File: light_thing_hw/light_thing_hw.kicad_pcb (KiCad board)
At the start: 2 copper layers, 51 parts, among them J1 CONNECTORS, J2 Li-Ion Battery, J3 ADDR_LED_PANEL_1_CONNECTORS, J4 ADDR_LED_PANEL_2_CONNECTORS, Q1 MMBF170, SW1 ST_USER_BUTTON1, SW2 ST_RESET_BUTTON, U1 BC832-V1, U2 LSM6DS3, U3 MCP73833T-FCI_MF, U4 LMR62421XMF, U5 LP38511MRX-ADJ_NOPB, U5A1 STM32L452RETx

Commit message: hw updates
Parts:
- moved J2 6.18 mm to (166.8, 80.5)
- moved SW1 4.24 mm to (155.0, 74.0)
- moved USB_MICRO_CONN1 4.24 mm to (154.9, 62.0)
- moved D2 3.16 mm to (161.0, 49.0)
- moved D3 3.16 mm to (156.9, 49.0)
- moved J1 3.16 mm to (174.0, 70.0)
- moved J3 3.16 mm to (169.0, 70.0)
- moved J4 3.16 mm to (165.0, 70.0)
- moved Q1 3.16 mm to (182.0, 63.0)
- moved SW2 3.16 mm to (160.0, 59.0)
- moved U1 3.16 mm to (176.0, 53.0)
- moved U2 3.16 mm to (181.0, 54.0)
- moved U3 3.16 mm to (181.0, 62.0)
- moved U4 3.16 mm to (180.0, 68.0)
- moved U5 3.16 mm to (182.0, 75.0)
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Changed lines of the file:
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@@
   (general
     (thickness 1.6)
-    (drawings 11)
+    (drawings 12)
     (tracks 0)
     (zones 0)
@@
   )
   (module LED_SMD:LED_1806_4516Metric_Pad1.57x1.80mm_HandSolder (layer F.Cu)
-    (at 164 50 90)
+    (at 161 49 90)
     (descr "LED SMD 1806 (4516 Metric), square (rectangular) end terminal, IPC_7351 nominal, (Body size source: https://www.modelithics.com/models/Vendor/MuRata/BLM41P.pdf), generated with kicad-footprint-generator")
     (tags "LED handsolder")
@@
   )
   (module LED_SMD:LED_1806_4516Metric_Pad1.57x1.80mm_HandSolder (layer F.Cu)
-    (at 159.9125 50 90)
+    (at 156.9125 49 90)
     (descr "LED SMD 1806 (4516 Metric), square (rectangular) end terminal, IPC_7351 nominal, (Body size source: https://www.modelithics.com/models/Vendor/MuRata/BLM41P.pdf), generated with kicad-footprint-generator")
     (tags "LED handsolder")
@@
   )
   (module Connector_Molex:Molex_PicoBlade_53261-0271_1x02-1MP_P1.25mm_Horizontal (layer B.Cu)
-    (at 172.825 79)
+    (at 166.825 80.5)
     (descr "Molex PicoBlade series connector, 53261-0271 (http://www.molex.com/pdm_docs/sd/532610271_sd.pdf), generated with kicad-footprint-generator")
     (tags "connector Molex PicoBlade top entry")
@@
   )
   (module Connector_PinHeader_1.00mm:PinHeader_2x02_P1.00mm_Vertical (layer F.Cu)
-    (at 172 71)
+    (at 169 70)
     (descr "Through hole straight pin header, 2x02, 1.00mm pitch, double rows")
     (tags "Through hole pin header THT 2x02 1.00mm double row")
@@
   )
   (module Connector_PinHeader_1.00mm:PinHeader_2x02_P1.00mm_Vertical (layer F.Cu)
-    (at 168 71)
+    (at 165 70)
     (descr "Through hole straight pin header, 2x02, 1.00mm pitch, double rows")
     (tags "Through hole pin header THT 2x02 1.00mm double row")
@@
   )
   (module Package_TO_SOT_SMD:SOT-23 (layer F.Cu)
-    (at 185 64)
+    (at 182 63)
     (descr "SOT-23, Standard")
     (tags SOT-23)
@@
   )
   (module Button_Switch_THT:SW_Tactile_SPST_Angled_PTS645Vx39-2LFS (layer B.Cu)
-    (at 158 71 270)
+    (at 155 74 270)
     (descr "tactile switch SPST right angle, PTS645VL39-2 LFS")
     (tags "tactile switch SPST angled PTS645VL39-2 LFS C&K Button")
@@
   )
   (module Button_Switch_SMD:SW_SPST_CK_RS282G05A3 (layer F.Cu)
-    (at 163 60 90)
+    (at 160 59 90)
     (descr https://www.mouser.com/ds/2/60/RS-282G05A-SM_RT-1159762.pdf)
     (tags "SPST button tactile switch")
@@
   )
   (module Package_LGA:LGA-14_3x2.5mm_P0.5mm_LayoutBorder3x4y (layer F.Cu)
-    (at 184 55)
+    (at 181 54)
     (descr "LGA, 14 Pin (http://www.st.com/resource/en/datasheet/lsm6ds3.pdf), generated with kicad-footprint-generator ipc_lga_layoutBorder_generator.py")
     (tags "LGA LGA")
@@
   )
   (module footprints:MCP73833T-FCI&slash_MF (layer B.Cu)
-    (at 184 63)
+    (at 181 62)
     (fp_text reference U3 (at 0 3) (layer B.SilkS)
       (effects (font (size 1 1) (thickness 0.15)) (justify mirror))
@@
   )
   (module Package_TO_SOT_SMD:SOT-23-5 (layer B.Cu)
-    (at 183 69)
+    (at 180 68)
     (descr "5-pin SOT23 package")
     (tags SOT-23-5)
@@
   )
   (module footprints:LP38511MRX-ADJ_NOPB (layer B.Cu)
-    (at 185 76)
+    (at 182 75)
     (fp_text reference U5 (at 0 0) (layer B.SilkS)
       (effects (font (size 1 1) (thickness 0.15)) (justify mirror))
@@
   )
   (module Package_QFP:LQFP-64-1EP_10x10mm_P0.5mm_EP6.5x6.5mm (layer F.Cu)
-    (at 174 60)
+    (at 171 59)
     (descr "64 LEAD LQFP 10x10mm (see MICREL LQFP10x10-64LD-PL-1.pdf and http://www.nxp.com/files/shared/doc/package_info/98ARH98426A.pdf for EP)")
     (tags "QFP 0.5")
@@
   )
   (module Connector_USB:USB_Micro-B_Molex_47346-0001 (layer B.Cu)
-    (at 157.9 59 90)
+    (at 154.9 62 90)
     (descr "Micro USB B receptable with flange, bottom-mount, SMD, right-angle (http://www.molex.com/pdm_docs/sd/473460001_sd.pdf)")
     (tags "Micro B USB SMD")
@@
   )
   (module Connector_PinHeader_1.00mm:PinHeader_2x05_P1.00mm_Vertical (layer F.Cu)
-    (at 177 71)
+    (at 174 70)
     (descr "Through hole straight pin header, 2x05, 1.00mm pitch, double rows")
     (tags "Through hole pin header THT 2x05 1.00mm double row")
@@
   )
   (module Fanstel_modules:BC832-BC832_3d1 (layer B.Cu)
-    (at 179 54 180)
+    (at 176 53 180)
     (attr smd)
     (fp_text reference U1 (at 4.3 9.7 180) (layer B.SilkS)
@@
     )
   )
-  (dimension 30 (width 0.3) (layer F.SilkS)
-    (gr_text "30.000 mm" (at 193.1 65 270) (layer F.SilkS)
+  (gr_line (start 151 48) (end 151 43) (layer F.SilkS) (width 0.2))
+  (gr_line (start 193 80) (end 193 85) (layer F.SilkS) (width 0.2))
+  (dimension 42 (width 0.3) (layer F.SilkS)
+    (gr_text "42.000 mm" (at 140.9 64 90) (layer F.SilkS)
       (effects (font (size 1.5 1.5) (thickness 0.3)))
     )
-    (feature1 (pts (xy 190 80) (xy 191.586421 80)))
-    (feature2 (pts (xy 190 50) (xy 191.586421 50)))
-    (crossbar (pts (xy 191 50) (xy 191 80)))
-    (arrow1a (pts (xy 191 80) (xy 190.413579 78.873496)))
-    (arrow1b (pts (xy 191 80) (xy 191.586421 78.873496)))
-    (arrow2a (pts (xy 191 50) (xy 190.413579 51.126504)))
-    (arrow2b (pts (xy 191 50) (xy 191.586421 51.126504)))
-  )
-  (gr_line (start 190 80) (end 190 50) (layer F.SilkS) (width 0.2))
-  (gr_line (start 160 80) (end 190 80) (layer F.SilkS) (width 0.2))
-  (gr_line (start 160 50) (end 160 80) (layer F.SilkS) (width 0.2))
-  (gr_line (start 190 50) (end 160 50) (layer F.SilkS) (width 0.2))
-  (dimension 40 (width 0.3) (layer F.SilkS)
-    (gr_text "40.000 mm" (at 199.1 65 90) (layer F.SilkS)
+    (feature1 (pts (xy 151 43) (xy 142.413579 43)))
+    (feature2 (pts (xy 151 85) (xy 142.413579 85)))
+    (crossbar (pts (xy 143 85) (xy 143 43)))
+    (arrow1a (pts (xy 143 43) (xy 143.586421 44.126504)))
+    (arrow1b (pts (xy 143 43) (xy 142.413579 44.126504)))
+    (arrow2a (pts (xy 143 85) (xy 143.586421 83.873496)))
+    (arrow2b (pts (xy 143 85) (xy 142.413579 83.873496)))
+  )
+  (gr_line (start 193 43) (end 151 43) (layer F.SilkS) (width 0.2))
+  (gr_line (start 193 80) (end 193 43) (layer F.SilkS) (width 0.2))
+  (gr_line (start 151 85) (end 193 85) (layer F.SilkS) (width 0.2))
+  (gr_line (start 151 48) (end 151 85) (layer F.SilkS) (width 0.2))
+  (dimension 42 (width 0.3) (layer F.SilkS)
+    (gr_text "42.000 mm" (at 172 92.1) (layer F.SilkS)
       (effects (font (size 1.5 1.5) (thickness 0.3)))
     )
-    (feature1 (pts (xy 197 45) (xy 197.586421 45)))
-    (feature2 (pts (xy 197 85) (xy 197.586421 85)))
-    (crossbar (pts (xy 197 85) (xy 197 45)))
-    (arrow1a (pts (xy 197 45) (xy 197.586421 46.126504)))
-    (arrow1b (pts (xy 197 45) (xy 196.413579 46.126504)))
-    (arrow2a (pts (xy 197 85) (xy 197.586421 83.873496)))
-    (arrow2b (pts (xy 197 85) (xy 196.413579 83.873496)))
-  )
-  (dimension 40 (width 0.3) (layer F.SilkS)
-    (gr_text "40.000 mm" (at 175 91.1) (layer F.SilkS)
-      (effects (font (size 1.5 1.5) (thickness 0.3)))
-    )
-    (feature1 (pts (xy 195 89) (xy 195 89.586421)))
-    (feature2 (pts (xy 155 89) (xy 155 89.586421)))
-    (crossbar (pts (xy 155 89) (xy 195 89)))
-    (arrow1a (pts (xy 195 89) (xy 193.873496 89.586421)))
-    (arrow1b (pts (xy 195 89) (xy 193.873496 88.413579)))
-    (arrow2a (pts (xy 155 89) (xy 156.126504 89.586421)))
-    (arrow2b (pts (xy 155 89) (xy 156.126504 88.413579)))
-  )
-  (gr_line (start 195 85) (end 195 45) (layer F.SilkS) (width 0.2))
-  (gr_line (start 155 85) (end 195 85) (layer F.SilkS) (width 0.2))
-  (gr_line (start 155 45) (end 155 85) (layer F.SilkS) (width 0.2))
-  (gr_line (start 195 45) (end 155 45) (layer F.SilkS) (width 0.2))
+    (feature1 (pts (xy 193 85) (xy 193 90.586421)))
+    (feature2 (pts (xy 151 85) (xy 151 90.586421)))
+    (crossbar (pts (xy 151 90) (xy 193 90)))
+    (arrow1a (pts (xy 193 90) (xy 191.873496 90.586421)))
+    (arrow1b (pts (xy 193 90) (xy 191.873496 89.413579)))
+    (arrow2a (pts (xy 151 90) (xy 152.126504 90.586421)))
+    (arrow2b (pts (xy 151 90) (xy 152.126504 89.413579)))
+  )
+  (gr_line (start 187 79) (end 187 49) (layer F.SilkS) (width 0.2))
+  (gr_line (start 157 79) (end 187 79) (layer F.SilkS) (width 0.2))
+  (gr_line (start 157 49) (end 157 79) (layer F.SilkS) (width 0.2))
+  (gr_line (start 187 49) (end 157 49) (layer F.SilkS) (width 0.2))
 )

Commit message: hw updates
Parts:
- removed 1k1: R, Resistor_SMD:R_0603_1608Metric_Pad1.05x0.95mm_HandSolder
- C10, C11, C12, C13, C14, C5, C6, C8, D1, L1, R1, R15, R16, R3, R4: moved to B.Cu
- R2: value 1M -> 1k
- moved R8 89.3 mm to (154.0, 68.9), turned to 270 degrees
- moved C10 86.8 mm to (165.0, 56.0), turned to 180 degrees
- moved C8 81.9 mm to (164.0, 64.9), turned to 270 degrees
- moved R5 78.4 mm to (168.1, 52.0), turned to 180 degrees
- moved C2 78.3 mm to (168.0, 46.6), turned to 90 degrees
- moved C13 77.0 mm to (165.0, 70.0)
- moved R9 76.0 mm to (154.0, 57.0), turned to 270 degrees
- moved C1 75.8 mm to (165.0, 46.6), turned to 90 degrees
- moved R3 75.5 mm to (168.0, 59.0), turned to 270 degrees
- moved C3 75.1 mm to (171.0, 46.6), turned to 90 degrees
- moved R2 68.2 mm to (167.0, 68.0), turned to 180 degrees
- moved D1 61.3 mm to (162.0, 60.0), turned to 270 degrees
- moved R1 60.2 mm to (186.1, 61.0)
- moved R15 60.1 mm to (178.0, 81.0), turned to 270 degrees
- moved R4 59.9 mm to (174.0, 59.0), turned to 90 degrees
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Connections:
- R2 pad 1: Net-(R2-Pad1) -> BATT_ADC
- U4 pad 4: Net-(R2-Pad1) -> BOOST_ENABLE
- U5A1 pad 38: Net-(U5A1-Pad38) -> BOOST_ENABLE
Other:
- board outline added: 42 x 42 mm

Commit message: made 5cm pcb. need to do routing etc.
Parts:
- added C15: 2700pF, Capacitor_SMD:C_0603_1608Metric_Pad1.05x0.95mm_HandSolder, B.Cu at (119.6, 70.1)
- added C18: 10uF, Capacitor_SMD:C_0603_1608Metric_Pad1.05x0.95mm_HandSolder, B.Cu at (119.6, 74.2)
- added R17: 1k, Resistor_SMD:R_0603_1608Metric_Pad1.05x0.95mm_HandSolder, B.Cu at (147.0, 73.1)
- C1, C16, C17, C2, C3, C4, R8, R9: moved to B.Cu
- D2, D3: footprint LED_SMD:LED_1806_4516Metric_Pad1.57x1.80mm_HandSolder -> LED_SMD:LED_0603_1608Metric_Pad1.05x0.95mm_HandSolder; moved to B.Cu
- R1: value 800 -> 1k
- R15: value 3.5k -> 2k
- R16: value 3.5k -> 357
- R6: value R -> 4.7k; moved to B.Cu
- R7: value R -> 100; moved to B.Cu
- SW1: footprint Button_Switch_THT:SW_Tactile_SPST_Angled_PTS645Vx39-2LFS -> Button_Switch_SMD:SW_SPST_B3U-3000P
- U3: value MCP73833T-FCI_MF -> MCP73833T-FCI_UN; footprint footprints:MCP73833T-FCI&slash_MF -> footprints:MCP73833T-FCIUN-SMD
- moved R7 74.5 mm to (110.5, 66.0)
- moved C17 73.9 mm to (131.8, 102.6)
- moved R6 73.7 mm to (110.5, 63.0)
- moved C16 70.1 mm to (134.8, 102.6)
- moved C4 66.7 mm to (137.8, 102.6)
- moved C3 63.6 mm to (140.8, 102.6)
- moved C2 61.0 mm to (143.8, 102.6)
- moved J2 59.2 mm to (111.8, 102.3)
- moved C1 58.9 mm to (146.8, 102.6)
- moved D3 58.9 mm to (127.9, 104.8), turned to 180 degrees
- moved R9 56.4 mm to (124.0, 104.8), turned to 180 degrees
- moved U5 55.8 mm to (126.2, 75.2)
- moved R15 55.7 mm to (122.3, 82.5)
- moved R16 55.7 mm to (126.3, 82.5)
- moved C14 55.7 mm to (130.3, 82.5)
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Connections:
- C1 pad 2: +5V -> GND
- C10 pad 2: +5V -> GND
- C11 pad 2: +5V -> GND
- C14 pad 2: +5V -> GND
- C16 pad 2: +5V -> GND
- C17 pad 2: +5V -> GND
- C2 pad 2: +5V -> GND
- C3 pad 2: +5V -> GND
- C4 pad 2: +5V -> GND
- C5 pad 2: +5V -> GND
- C6 pad 2: +5V -> Net-(C6-Pad2)
- C7 pad 2: +5V -> GND
- C8 pad 1: +5V -> GND
- C9 pad 2: +5V -> GND
- D2 pad 1: +5V -> GND
- D3 pad 1: +5V -> GND
- J2 pad 1: +5V -> GND
- J3 pad 1: +5V -> GND
- J3 pad 4: +5V -> GND
- J4 pad 1: +5V -> GND
- J4 pad 4: +5V -> GND
- Q1 pad 2: +5V -> GND
- R1 pad 1: +5V -> VBUS
- R16 pad 1: +5V -> GND
- R4 pad 2: +5V -> GND
- R5 pad 2: +5V -> GND
- R6 pad 2: +5V -> GND
- R7 pad 1: +5V -> GND
- SW1 pad 1: +5V -> GND
- SW2 pad 1: +5V -> GND
- U1 pad P$1: +5V -> GND
- U2 pad 1: +5V -> GND
- U2 pad 2: +5V -> GND
- U2 pad 3: +5V -> GND
- U2 pad 6: +5V -> GND
- U2 pad 7: +5V -> GND
- U3 pad 10: +BATT -> Net-(C6-Pad2)
- U3 pad 3: Net-(U3-Pad3) -> CHARGER_STAT1
- U3 pad 4: Net-(U3-Pad4) -> CHARGER_STAT2
- U3 pad 5: +5V -> GND
- U3 pad 6: Net-(R1-Pad2) -> Net-(R17-Pad2)
- U3 pad 7: Net-(U3-Pad7) -> Net-(R1-Pad2)
- U3 pad 9: +BATT -> Net-(C6-Pad2)
- U4 pad 2: +5V -> GND
- U5 pad 5: +5V -> GND
- U5 pad 9: +5V -> GND
- U5A1 pad 12: +5V -> GND
- U5A1 pad 18: +5V -> GND
- U5A1 pad 30: Net-(U5A1-Pad30) -> I2C2_SDA
- U5A1 pad 31: +5V -> GND
- U5A1 pad 35: I2C2_SDA -> CHARGER_STAT1
- U5A1 pad 36: Net-(U5A1-Pad36) -> CHARGER_STAT2
- U5A1 pad 47: +5V -> GND
- U5A1 pad 63: +5V -> GND
- USB_MICRO_CONN1 pad 5: +5V -> GND
- USB_MICRO_CONN1 pad 6: Net-(USB_MICRO_CONN1-Pad6) -> GND
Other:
- board size 42 x 42 mm -> 50 x 50 mm
- board text added: "L i g h t C u b e - HwVer:1"

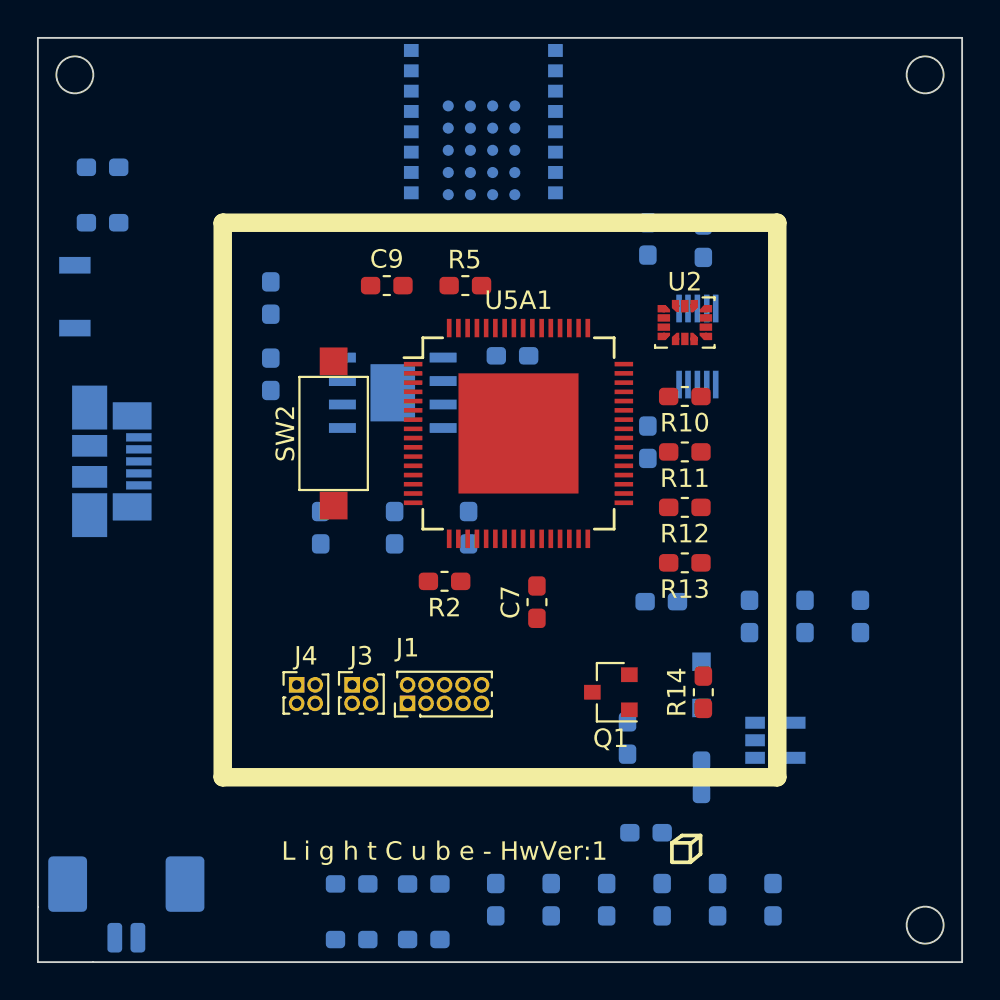
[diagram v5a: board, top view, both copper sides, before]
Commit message: hw updates. sw initd new needed peripherals. some changes on pixel testbench
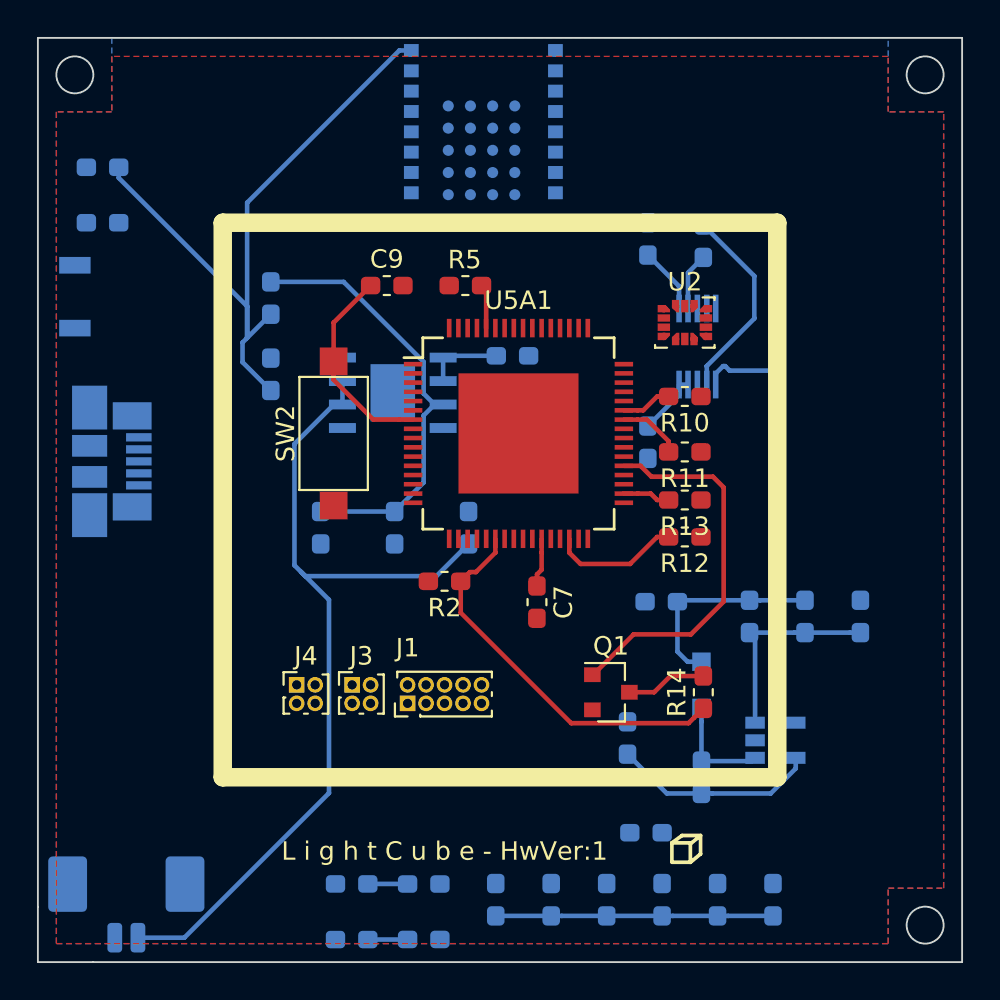
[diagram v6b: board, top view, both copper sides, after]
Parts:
- moved R13 3.40 mm to (142.0, 81.0)
- moved R12 1.60 mm to (142.0, 83.0)
- turned C7 to 270 degrees
- turned Q1 to 0 degrees
- turned R6 to 180 degrees
- turned U5 to 180 degrees
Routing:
- net +BATT: track 0.00 -> 59.0 mm
- net +3V3: track 0.00 -> 56.3 mm
- net Net-(C15-Pad1): track 0.00 -> 23.8 mm
- net BATT_ADC: track 0.00 -> 20.9 mm
- net BATT_ADC_ENABLE: track 0.00 -> 20.8 mm
- net +5V: track 0.00 -> 11.2 mm
- net RESET: track 0.00 -> 11.1 mm
- net Net-(C12-Pad2): track 0.00 -> 11.0 mm
- net Net-(R1-Pad2): track 0.00 -> 10.8 mm
- net I2C2_SDA: track 0.00 -> 6.98 mm
- net VBUS: track 0.00 -> 6.70 mm
- net Net-(D1-Pad2): track 0.00 -> 5.85 mm
- net Net-(Q1-Pad3): track 0.00 -> 4.36 mm
- net Net-(R17-Pad2): track 0.00 -> 4.20 mm
- net I2C1_SCL: track 0.00 -> 3.49 mm
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- added copper zone on B.Cu, net GND
- added copper zone on F.Cu, net GND

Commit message: redone layout
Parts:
- C1, C11, C13, C16, C17, C2, C3, C4, R7: moved to F.Cu
- Q1, R14, R2: moved to B.Cu
- U5: value LP38511MRX-ADJ_NOPB -> LP38511MRX
- moved D3 43.2 mm to (111.0, 65.0), turned to 90 degrees
- moved R9 42.1 mm to (114.8, 63.6), turned to 0 degrees
- moved R8 41.8 mm to (114.8, 61.0), turned to 0 degrees
- moved D2 41.3 mm to (109.0, 65.0), turned to 90 degrees
- moved C1 37.8 mm to (126.0, 71.0)
- moved C2 35.3 mm to (128.0, 71.0)
- moved C3 33.4 mm to (130.0, 71.0)
- moved C13 33.3 mm to (123.9, 69.8), turned to 90 degrees
- moved U1 32.9 mm to (142.4, 97.1), turned to 0 degrees
- moved C4 32.1 mm to (132.0, 71.0)
- moved C17 31.9 mm to (136.0, 71.0)
- moved C16 31.6 mm to (134.0, 71.0)
- moved R14 31.2 mm to (112.0, 94.9)
- moved U4 29.4 mm to (121.1, 80.0), turned to 180 degrees
- moved Q1 27.0 mm to (111.0, 90.0)
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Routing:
- net +BATT: track 59.0 -> 0.00 mm
- net +3V3: track 56.3 -> 0.00 mm
- net Net-(C15-Pad1): track 23.8 -> 0.00 mm
- net BATT_ADC: track 20.9 -> 0.00 mm
- net BATT_ADC_ENABLE: track 20.8 -> 0.00 mm
- net +5V: track 11.2 -> 0.00 mm
- net RESET: track 11.1 -> 0.00 mm
- net Net-(C12-Pad2): track 11.0 -> 0.00 mm
- net Net-(R1-Pad2): track 10.8 -> 0.00 mm
- net I2C2_SDA: track 6.98 -> 0.00 mm
- net VBUS: track 6.70 -> 0.00 mm
- net Net-(D1-Pad2): track 5.85 -> 0.00 mm
- net Net-(Q1-Pad3): track 4.36 -> 0.00 mm
- net Net-(R17-Pad2): track 4.20 -> 0.00 mm
- net I2C1_SCL: track 3.49 -> 0.00 mm
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- removed copper zone on B.Cu, net GND
- removed copper zone on F.Cu, net GND
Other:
- outline, holes or cut-outs redrawn
- board text added: "BLE"
- board text added: "ST"
